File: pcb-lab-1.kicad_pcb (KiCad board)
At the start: 2 copper layers, 60 parts, among them J1 BAT, J10 JP_RX, J11 JP_TX, J14 JP_RX, J15 JP_TX, J18 UART, J2 UPDI_PIN_SMD, J20 UPDI, Q30 NMOS_GSD, Q31 NMOS_GSD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

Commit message: Component arrangement
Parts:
- added C8: 1u, Capacitor_SMD:C_0805_2012Metric, F.Cu at (148.5, 74.5)
- C4: value 100nF -> 100n
- moved R3 42.4 mm to (150.3, 97.5), turned to 90 degrees
- moved R2 41.9 mm to (152.9, 97.5), turned to 90 degrees
- moved R1 41.7 mm to (155.4, 97.5), turned to 90 degrees
- moved C21 40.0 mm to (179.0, 103.0), turned to 0 degrees
- moved C20 39.4 mm to (175.0, 103.0), turned to 180 degrees
- moved D3 35.6 mm to (150.3, 92.8), turned to 90 degrees
- moved D2 35.0 mm to (152.9, 92.8), turned to 90 degrees
- moved D1 34.8 mm to (155.4, 92.8), turned to 90 degrees
- moved U20 33.6 mm to (177.0, 100.0)
- moved JST_PH_BAT1 32.4 mm to (106.7, 99.7), turned to 270 degrees
- moved J20 31.0 mm to (195.6, 91.4)
- moved J15 30.7 mm to (185.4, 76.2)
- moved JP20 30.7 mm to (165.1, 91.4), turned to 180 degrees
- moved R20 30.1 mm to (192.0, 97.0)
- moved JD1 29.7 mm to (124.5, 76.2), turned to 180 degrees
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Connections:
- U11 pad 6: Net-(U11-Pad6) -> 5V
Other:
- board outline added: 95.3 x 33 mm

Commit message: New netlist, and approx pcb arrangement
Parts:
- added JP1: jumper, local_footprints:Pin_Header_Straight_1x02_Pitch2.54mm, F.Cu at (116.8, 96.5)
- added JP2: ADC, local_footprints:Pin_Header_Straight_1x03_Pitch2.54mm, F.Cu at (147.3, 86.4)
- added R8: 100k, Resistor_SMD:R_0603_1608Metric, F.Cu at (119.5, 94.0)
- added R9: 100k, Resistor_SMD:R_0603_1608Metric, F.Cu at (119.5, 99.0)
- added U6: 74LVC1G3157, local_footprints:SOT-23-6_HS, F.Cu at (127.0, 88.0)
- C1: value 10uF -> 10u
- C10, C11, C12, C13, C14, C15, C2, C20, C21, C3, C30, C31: value 100nF -> 100n
- C5: value 1uF -> 1u
- C6, C7: value 0.1uF -> 100n
- moved SW1 15.5 mm to (153.0, 103.0)
- moved JP30 5.08 mm to (142.2, 96.5)
- moved JP31 5.08 mm to (144.8, 96.5)
- moved JP32 5.08 mm to (127.0, 96.5)
- moved JP33 5.08 mm to (124.5, 96.5)
- moved R6 3.50 mm to (143.0, 81.5), turned to 90 degrees
- moved JD1 2.54 mm to (124.5, 73.7)
- moved R7 2.50 mm to (141.0, 81.5), turned to 270 degrees
- moved C8 1.58 mm to (150.0, 74.0)
- moved C4 1.50 mm to (154.0, 74.5)
- moved C7 1.50 mm to (148.0, 78.0)
- moved U2 1.36 mm to (154.0, 80.2)
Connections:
- R6 pad 2: VBAT_ADC -> VBAT_ADC_A
- R7 pad 1: VBAT_ADC -> VBAT_ADC_A

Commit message: New component arrangement
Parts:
- moved JP1 27.4 mm to (142.2, 86.4), turned to 180 degrees
- moved R9 26.4 mm to (145.0, 92.0), turned to 90 degrees
- moved R8 23.6 mm to (143.0, 92.0), turned to 270 degrees
- moved U6 19.0 mm to (146.0, 87.5)
- moved R4 11.7 mm to (162.0, 93.0)
- moved JP2 7.73 mm to (154.9, 87.6)
- moved JST_PH_BAT1 3.82 mm to (110.5, 99.5)
- moved BT1 3.31 mm to (112.5, 84.9)
- moved J2 2.72 mm to (162.0, 89.5)
- moved SW1 2.55 mm to (155.5, 103.5)
- moved J1 2.54 mm to (114.3, 99.1)
- moved D1 2.50 mm to (157.9, 92.8)
- moved D2 2.50 mm to (155.4, 92.8)
- moved D3 2.50 mm to (152.8, 92.8)
- moved R1 2.50 mm to (157.9, 97.5)
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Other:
- board size 95.3 x 33 mm -> 91.4 x 33 mm

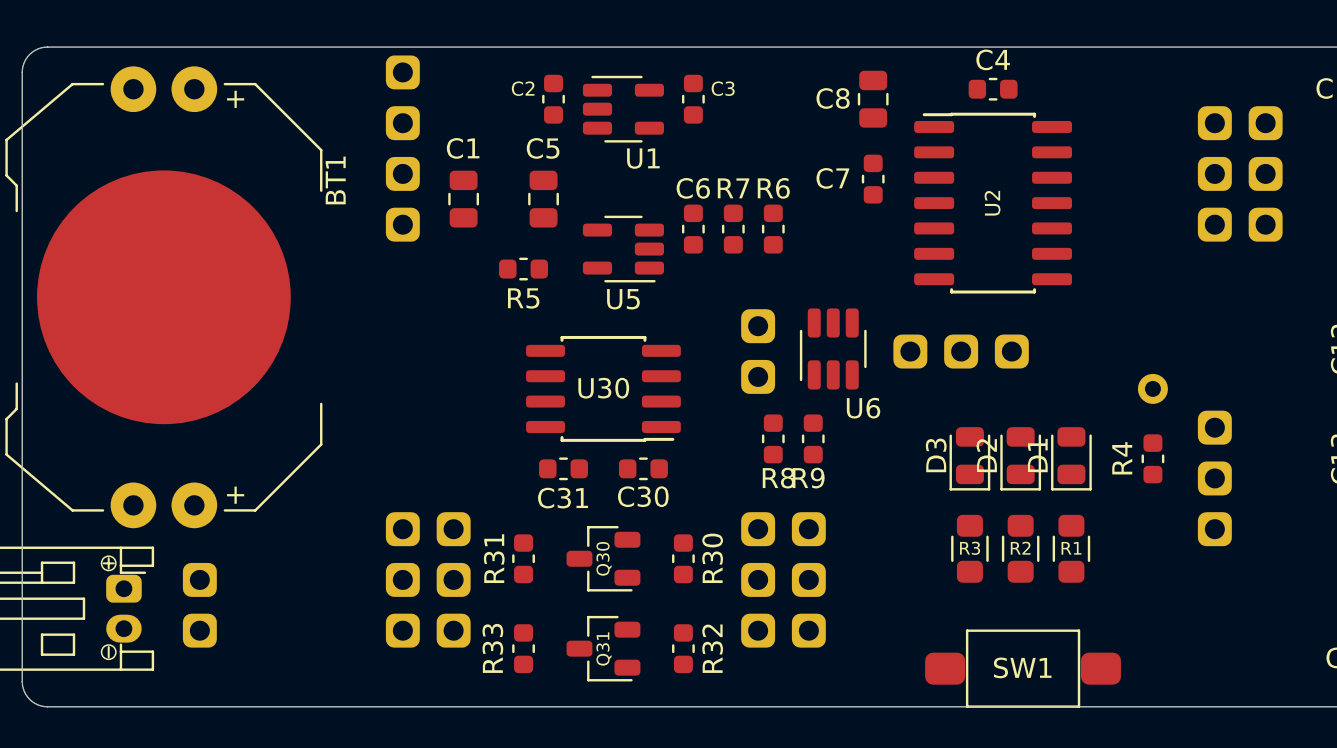
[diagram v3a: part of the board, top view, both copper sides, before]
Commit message: VBAT and I2C routing
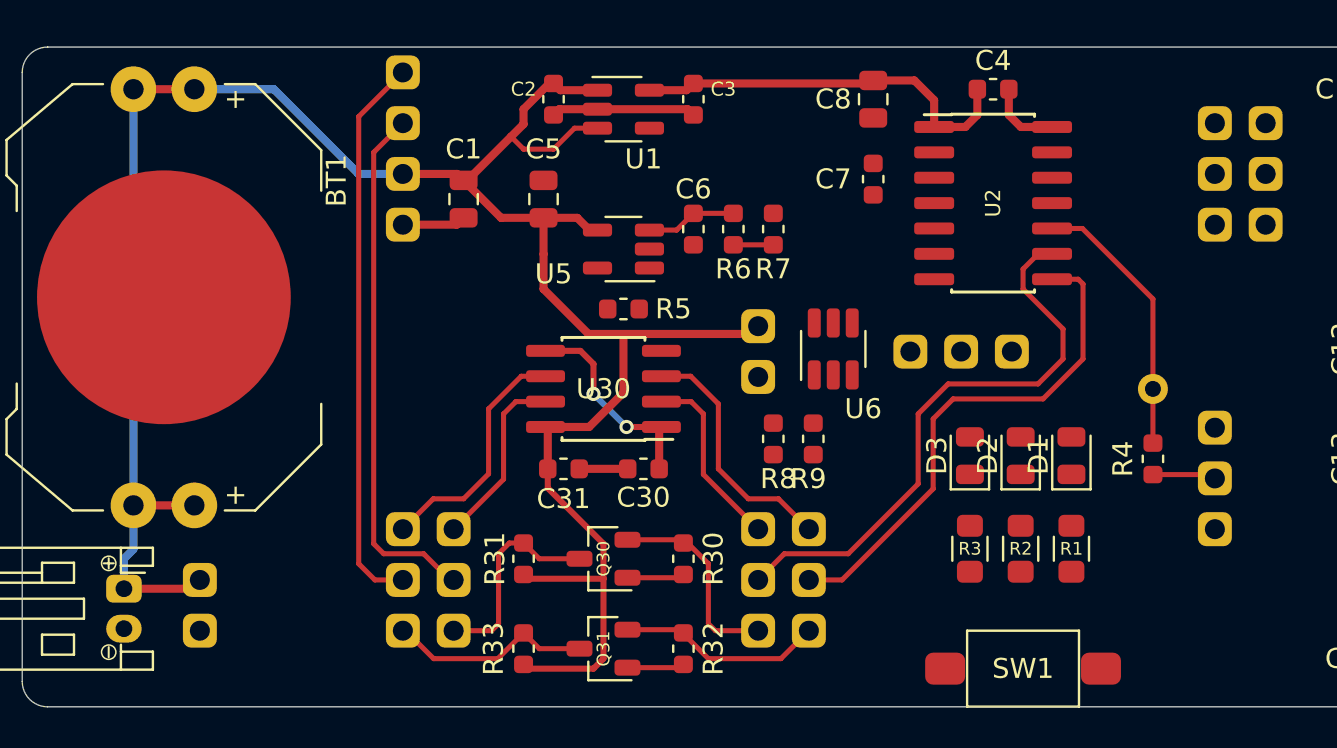
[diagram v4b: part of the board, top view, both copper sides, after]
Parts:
- moved R5 5.39 mm to (135.5, 85.5)
- moved R6 2.00 mm to (141.0, 81.5), turned to 270 degrees
- moved R7 2.00 mm to (143.0, 81.5), turned to 90 degrees
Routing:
- net VBAT: track 0.00 -> 117.9 mm
- net 2V5: track 0.00 -> 36.0 mm, vias 0 -> 2
- net SCL_2V5: track 0.00 -> 29.0 mm
- net SDA: track 0.00 -> 28.1 mm
- net SCL: track 0.00 -> 26.4 mm
- net SDA_2V5: track 0.00 -> 25.8 mm
- net GND: track 0.00 -> 16.5 mm
- net Net-(J2-Pad1): track 0.00 -> 13.7 mm
- net SDA_2V5_A: track 0.00 -> 12.5 mm
- net SDA_A: track 0.00 -> 12.2 mm
- net SCL_B: track 0.00 -> 10.5 mm
- net SDA_2V5_B: track 0.00 -> 10.3 mm
- net SDA_B: track 0.00 -> 10.3 mm
- net SCL_2V5_B: track 0.00 -> 10.2 mm
- net SCL_2V5_A: track 0.00 -> 9.26 mm
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
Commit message: Complete routing
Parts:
- moved D1 1.60 mm to (158.0, 94.4)
- moved R1 1.60 mm to (158.0, 99.1)
- moved D2 1.60 mm to (155.5, 94.4)
- moved D3 1.60 mm to (152.9, 94.4)
- moved R2 1.60 mm to (155.5, 99.1)
- moved R3 1.60 mm to (152.9, 99.1)
- moved J2 0.86 mm to (162.7, 90.0)
- moved R4 0.71 mm to (162.7, 92.9)
- turned C14 to 270 degrees
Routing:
- net 2V5: track 36.0 -> 166.9 mm, vias 2 -> 14
- net 5V: track 0.00 -> 80.9 mm, vias 0 -> 12
- net GND: track 16.5 -> 79.1 mm, vias 0 -> 41
- net Net-(SW1-Pad2): track 0.00 -> 28.8 mm, vias 0 -> 4
- net VCTRL: track 0.00 -> 22.6 mm, vias 0 -> 2
- net TX_2V5_B: track 0.00 -> 20.8 mm, vias 0 -> 2
- net Net-(D1-Pad2): track 0.00 -> 20.3 mm, vias 0 -> 2
- net Net-(D2-Pad2): track 0.00 -> 20.0 mm, vias 0 -> 2
- net Net-(D3-Pad2): track 0.00 -> 19.7 mm, vias 0 -> 2
- net TX_B: track 0.00 -> 19.2 mm, vias 0 -> 2
- net RX_2V5: track 0.00 -> 18.2 mm, vias 0 -> 2
- net TX_2V5: track 0.00 -> 18.1 mm, vias 0 -> 2
- net UPDI_A: track 0.00 -> 16.5 mm
- net RX_B: track 0.00 -> 16.3 mm, vias 0 -> 2
- net VBAT_ADC_A: track 2.00 -> 16.9 mm, vias 0 -> 4
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- added copper zone on B.Cu, net GND
